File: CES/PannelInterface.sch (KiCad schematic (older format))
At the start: 0 parts

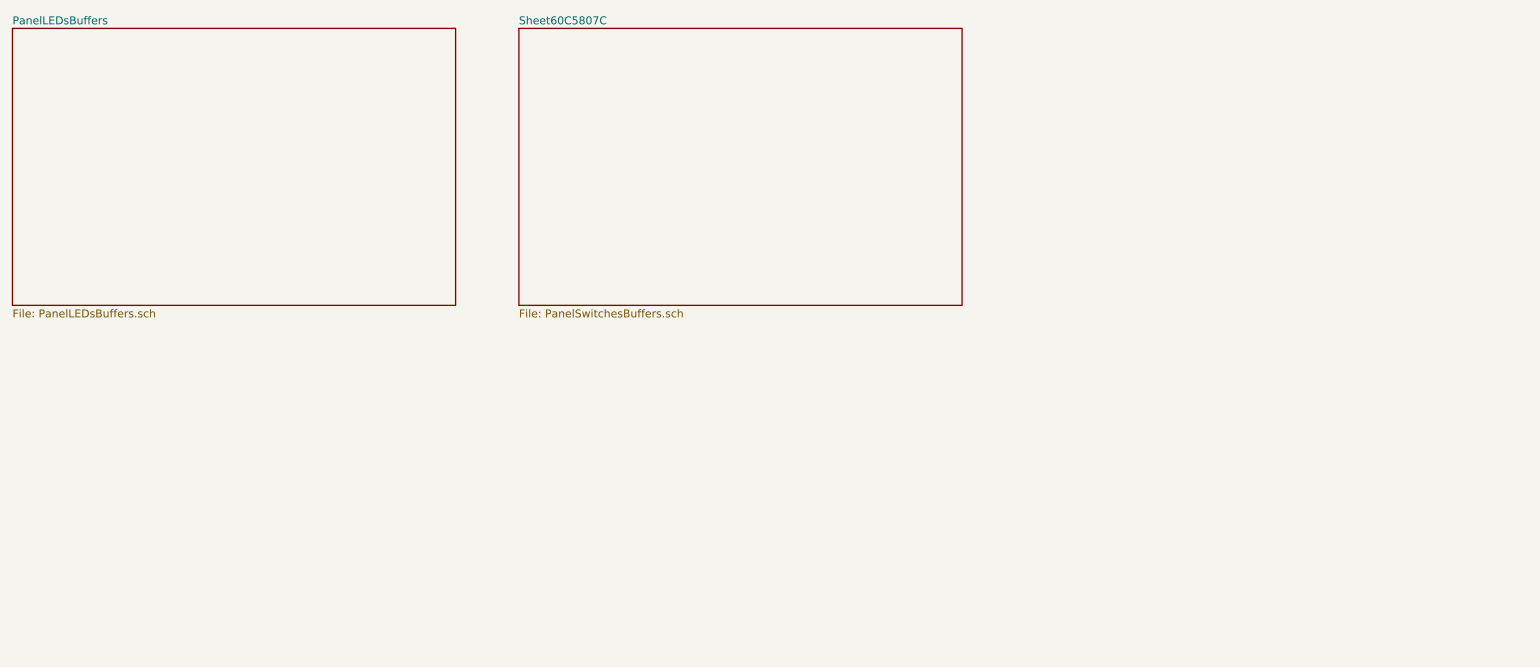
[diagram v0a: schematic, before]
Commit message: Address decoding. Clock. Pannel buttons
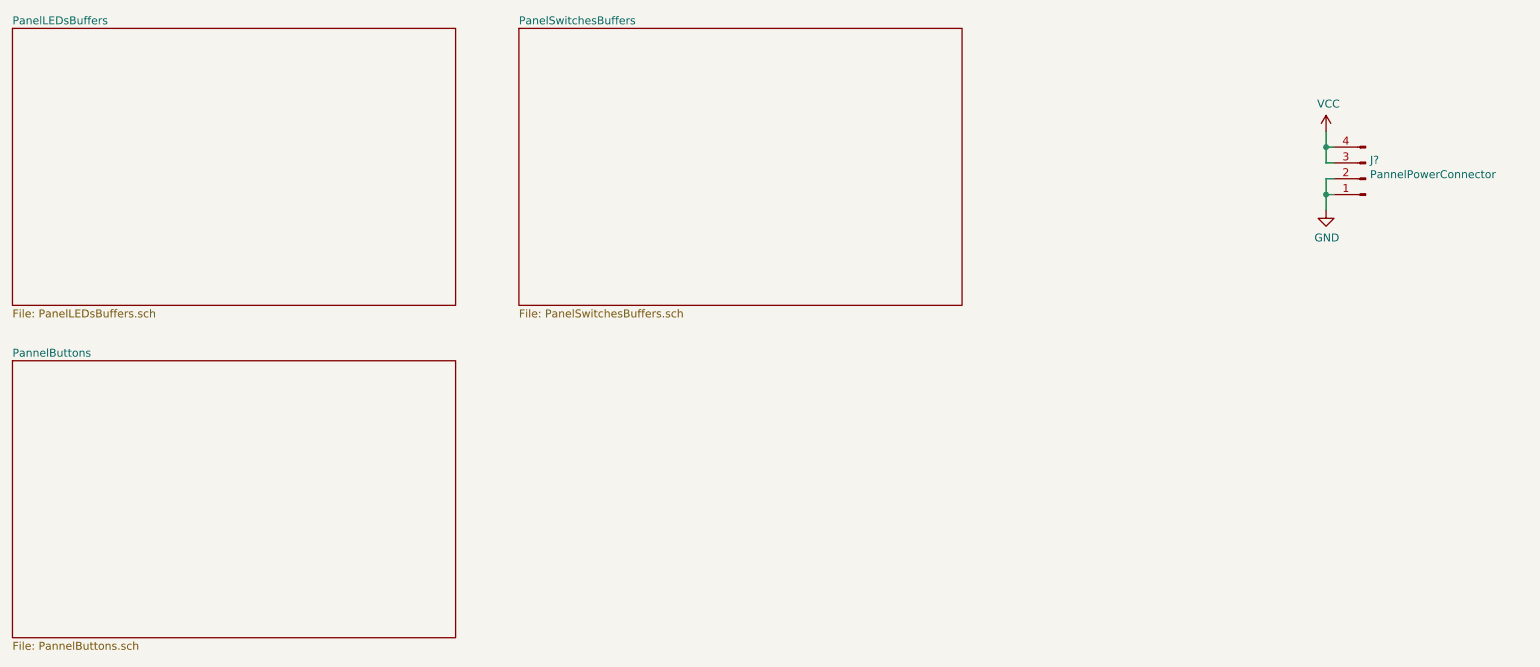
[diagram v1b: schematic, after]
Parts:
- added J?: PannelPowerConnector, symbol Connector:Conn_01x04_Male
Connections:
- new net GND: J?.1 (Pin_1), J?.2 (Pin_2)
- new net VCC: J?.3 (Pin_3), J?.4 (Pin_4)
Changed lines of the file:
@@
 $Descr A4 11693 8268
 encoding utf-8
-Sheet 11 13
+Sheet 11 15
 Title "CES"
 Date "2021-04-24"
@@
 S 3950 850  2800 1750
 U 60C5807D
-F0 "Sheet60C5807C" 50
+F0 "PanelSwitchesBuffers" 50
 F1 "PanelSwitchesBuffers.sch" 50
 $EndSheet
+$Comp
+L Connector:Conn_01x04_Male J?
+U 1 1 6124E597
+P 9300 1800
+F 0 "J?" H 9272 1682 50  0000 R CNN
+F 1 "PannelPowerConnector" H 9272 1773 50  0000 R CNN
+F 2 "" H 9300 1800 50  0001 C CNN
+F 3 "~" H 9300 1800 50  0001 C CNN
+	1    9300 1800
+	-1   0    0    1
+$EndComp
+Wire Wire Line
+	9100 1700 9050 1700
+Wire Wire Line
+	9050 1700 9050 1600
+Wire Wire Line
+	9050 1600 9100 1600
+Wire Wire Line
+	9100 1800 9050 1800
+Wire Wire Line
+	9050 1800 9050 1900
+Wire Wire Line
+	9050 1900 9100 1900
+$Comp
+L power:VCC #PWR?
+U 1 1 6124F639
+P 9050 1500
+F 0 "#PWR?" H 9050 1350 50  0001 C CNN
+F 1 "VCC" H 9065 1673 50  0000 C CNN
+F 2 "" H 9050 1500 50  0001 C CNN
+F 3 "" H 9050 1500 50  0001 C CNN
+	1    9050 1500
+	1    0    0    -1
+$EndComp
+$Comp
+L power:GND #PWR?
+U 1 1 6124F918
+P 9050 2000
+F 0 "#PWR?" H 9050 1750 50  0001 C CNN
+F 1 "GND" H 9055 1827 50  0000 C CNN
+F 2 "" H 9050 2000 50  0001 C CNN
+F 3 "" H 9050 2000 50  0001 C CNN
+	1    9050 2000
+	1    0    0    -1
+$EndComp
+Wire Wire Line
+	9050 1900 9050 2000
+Connection ~ 9050 1900
+Wire Wire Line
+	9050 1600 9050 1500
+Connection ~ 9050 1600
+$Sheet
+S 750  2950 2800 1750
+U 6125152F
+F0 "PannelButtons" 50
+F1 "PannelButtons.sch" 50
+$EndSheet
 $EndSCHEMATC

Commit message: Control Unit
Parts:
- gave numbers to parts that had none: 1
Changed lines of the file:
@@
 $Descr A4 11693 8268
 encoding utf-8
-Sheet 11 16
+Sheet 11 17
 Title "CES"
 Date "2021-04-24"
@@
 $EndSheet
 $Comp
-L Connector:Conn_01x04_Male J?
+L Connector:Conn_01x04_Male J1201
 U 1 1 6124E597
 P 9300 1800
-F 0 "J?" H 9272 1682 50  0000 R CNN
+F 0 "J1201" H 9272 1682 50  0000 R CNN
 F 1 "PannelPowerConnector" H 9272 1773 50  0000 R CNN
 F 2 "" H 9300 1800 50  0001 C CNN
@@
 	9050 1900 9100 1900
 $Comp
-L power:VCC #PWR?
+L power:VCC #PWR01201
 U 1 1 6124F639
 P 9050 1500
-F 0 "#PWR?" H 9050 1350 50  0001 C CNN
+F 0 "#PWR01201" H 9050 1350 50  0001 C CNN
 F 1 "VCC" H 9065 1673 50  0000 C CNN
 F 2 "" H 9050 1500 50  0001 C CNN
@@
 $EndComp
 $Comp
-L power:GND #PWR?
+L power:GND #PWR01202
 U 1 1 6124F918
 P 9050 2000
-F 0 "#PWR?" H 9050 1750 50  0001 C CNN
+F 0 "#PWR01202" H 9050 1750 50  0001 C CNN
 F 1 "GND" H 9055 1827 50  0000 C CNN
 F 2 "" H 9050 2000 50  0001 C CNN

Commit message: Assigning footprints and generating netlist
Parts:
- J1201: footprint (none) -> Connector_PinHeader_2.54mm:PinHeader_1x04_P2.54mm_Vertical
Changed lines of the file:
@@
 F 0 "J1201" H 9272 1682 50  0000 R CNN
 F 1 "PannelPowerConnector" H 9272 1773 50  0000 R CNN
-F 2 "" H 9300 1800 50  0001 C CNN
+F 2 "Connector_PinHeader_2.54mm:PinHeader_1x04_P2.54mm_Vertical" H 9300 1800 50  0001 C CNN
 F 3 "~" H 9300 1800 50  0001 C CNN
 	1    9300 1800
